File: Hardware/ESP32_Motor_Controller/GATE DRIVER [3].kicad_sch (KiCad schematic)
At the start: 42 parts, among them U301 DRV8302DCAR

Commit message: Test firmware
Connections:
- net PVDD: now also C314.1, C315.1, U301.53 (PVDD2), U301.54 (PVDD2)
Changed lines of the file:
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@@
+	)
+	(symbol
+		(lib_id "power:VSS")
+		(at 143.51 66.04 0)
+		(unit 1)
+		(exclude_from_sim no)
+		(in_bom yes)
+		(on_board yes)
+		(dnp no)
+		(property "Reference" "#PWR094"
+			(at 143.51 69.85 0)
+			(effects
+				(font
+					(size 1.27 1.27)
+				)
+				(hide yes)
+			)
+		)
+		(property "Value" "PVDD"
+			(at 147.32 64.516 0)
+			(effects
+				(font
+					(size 1.27 1.27)
+				)
+			)
+		)
+		(property "Footprint" ""
+			(at 143.51 66.04 0)
+			(effects
+				(font
+					(size 1.27 1.27)
+				)
+				(hide yes)
+			)
+		)
+		(property "Datasheet" ""
+			(at 143.51 66.04 0)
+			(effects
+				(font
+					(size 1.27 1.27)
+				)
+				(hide yes)
+			)
+		)
+		(property "Description" "Power symbol creates a global label with name \"VSS\""
+			(at 143.51 66.04 0)
+			(effects
+				(font
+					(size 1.27 1.27)
+				)
+				(hide yes)
+			)
+		)
+		(pin "1"
+		)
+		(instances
+			(project "ESP32_Motor_Controller"
+				(path "/4b1fdcf1-a19d-4728-9a21-4ed82cf33882/b48d869c-27f1-41d9-9235-2b29afe5c618"
+					(reference "#PWR094")
+					(unit 1)
+				)
+			)
+		)
 	)
 	(symbol
@@
 		(dnp no)
 		(property "Reference" "C315"
-			(at 140.716 64.262 0)
-			(effects
-				(font
+			(at 137.16 74.168 0)
+			(effects
+				(font

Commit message: PCB V2, CAD V3 & Code
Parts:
- C302, C311, C312, C313, C314, C315: footprint Capacitor_SMD:C_0402_1005Metric -> Capacitor_SMD:C_0805_2012Metric
- C320: footprint Capacitor_SMD:C_0402_1005Metric -> Capacitor_SMD:C_0603_1608Metric
- R311: value 3.3k -> 6.8k
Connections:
- net AGND: now also U301.28 (AGND)
- net at C313.1, U301.27 (AVDD): no longer U301.28 (AGND)
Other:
- note added: "90A x 2.4mΩ = 0.22V"
- note removed: "40A x 2.4mΩ = 0.1V"
- moved on the sheet: C313
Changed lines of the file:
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@@
 		)
 	)
-	(text "40A x 2.4mΩ = 0.1V\n"
+	(text "90A x 2.4mΩ = 0.22V\n"
 		(exclude_from_sim no)
 		(at 50.8 101.6 0)
@@
 	)
 	(junction
+		(at 147.32 156.21)
+		(diameter 0)
+		(color 0 0 0 0)
+	)
+	(junction
 		(at 64.77 60.96)
 		(diameter 0)
@@
 	)
 	(junction
-		(at 147.32 151.13)
-		(diameter 0)
-		(color 0 0 0 0)
-	)
-	(junction
 		(at 180.34 58.42)
 		(diameter 0)
@@
 	(wire
 		(pts
-			(xy 138.43 151.13) (xy 147.32 151.13)
+			(xy 62.23 107.95) (xy 92.71 107.95)
 		)
 		(stroke
@@
 	(wire
 		(pts
-			(xy 62.23 107.95) (xy 92.71 107.95)
+			(xy 147.32 156.21) (xy 147.32 158.75)
 		)
 		(stroke
@@
 	(wire
 		(pts
+			(xy 147.32 153.67) (xy 147.32 156.21)
+		)
+		(stroke
+			(width 0)
+			(type default)
+		)
+	)
+	(wire
+		(pts
 			(xy 29.21 102.87) (xy 41.91 102.87)
 		)
@@
 	(wire
 		(pts
+			(xy 138.43 151.13) (xy 143.51 151.13)
+		)
+		(stroke
+			(width 0)
+			(type default)
+		)
+	)
+	(wire
+		(pts
 			(xy 66.04 45.72) (xy 72.39 45.72)
 		)
@@
 	(wire
 		(pts
+			(xy 143.51 151.13) (xy 143.51 156.21)
+		)
+		(stroke
+			(width 0)
+			(type default)
+		)
+	)
+	(wire
+		(pts
 			(xy 80.01 68.58) (xy 80.01 69.85)
 		)
@@
 	(wire
 		(pts
-			(xy 161.29 87.63) (xy 170.18 87.63)
+			(xy 143.51 57.15) (xy 143.51 66.04)
 		)
 		(stroke
@@
 	(wire
 		(pts
-			(xy 147.32 148.59) (xy 147.32 151.13)
+			(xy 161.29 87.63) (xy 170.18 87.63)
 		)
 		(stroke
@@
 	(wire
 		(pts
-			(xy 147.32 151.13) (xy 147.32 153.67)
+			(xy 180.34 66.04) (xy 180.34 64.77)
 		)
 		(stroke
@@
 	(wire
 		(pts
-			(xy 180.34 66.04) (xy 180.34 64.77)
+			(xy 62.23 128.27) (xy 62.23 129.54)
 		)
 		(stroke
@@
 	(wire
 		(pts
-			(xy 62.23 128.27) (xy 62.23 129.54)
+			(xy 156.21 74.93) (xy 156.21 76.2)
 		)
 		(stroke
@@
 	(wire
 		(pts
-			(xy 156.21 74.93) (xy 156.21 76.2)
+			(xy 138.43 121.92) (xy 139.7 121.92)
 		)
 		(stroke
@@
 	(wire
 		(pts
-			(xy 138.43 121.92) (xy 139.7 121.92)
+			(xy 167.64 107.95) (xy 167.64 110.49)
 		)
 		(stroke
@@
 	(wire
 		(pts
-			(xy 167.64 107.95) (xy 167.64 110.49)
+			(xy 64.77 68.58) (xy 64.77 69.85)
 		)
 		(stroke
@@
 	(wire
 		(pts
-			(xy 64.77 68.58) (xy 64.77 69.85)
+			(xy 146.05 72.39) (xy 146.05 71.12)
 		)
 		(stroke
@@
 	(wire
 		(pts
-			(xy 146.05 72.39) (xy 146.05 71.12)
+			(xy 143.51 156.21) (xy 147.32 156.21)
 		)
 		(stroke
@@
 	(symbol
 		(lib_id "power:VSS")
-		(at 143.51 66.04 0)
+		(at 143.51 57.15 0)
 		(unit 1)
 		(exclude_from_sim no)
@@
 		(dnp no)
 		(property "Reference" "#PWR094"
-			(at 143.51 69.85 0)
+			(at 143.51 60.96 0)
 			(effects
 				(font
@@
 		)
 		(property "Value" "PVDD"
-			(at 147.32 64.516 0)
+			(at 147.32 55.626 0)
 			(effects
 				(font
@@
 		)
 		(property "Footprint" ""
-			(at 143.51 66.04 0)
+			(at 143.51 57.15 0)
 			(effects
 				(font
@@
 		)
 		(property "Datasheet" ""
-			(at 143.51 66.04 0)
+			(at 143.51 57.15 0)
 			(effects
 				(font
@@
 		)
 		(property "Description" "Power symbol creates a global label with name \"VSS\""
-			(at 143.51 66.04 0)
+			(at 143.51 57.15 0)
 			(effects
 				(font
@@
 			)
 		)
-		(property "Footprint" "Capacitor_SMD:C_0402_1005Metric"
+		(property "Footprint" "Capacitor_SMD:C_0805_2012Metric"
 			(at 143.51 68.58 0)
 			(effects
@@
 			)
 		)
-		(property "Value" "3.3k"
+		(property "Value" "6.8k"
 			(at 34.544 108.204 0)
 			(effects
@@
 			)
 		)
-		(property "Footprint" "Capacitor_SMD:C_0402_1005Metric"
+		(property "Footprint" "Capacitor_SMD:C_0805_2012Metric"
 			(at 175.26 62.23 0)
 			(effects
@@
 			)
 		)
-		(property "Footprint" "Capacitor_SMD:C_0402_1005Metric"
+		(property "Footprint" "Capacitor_SMD:C_0603_1608Metric"
 			(at 156.21 151.13 0)
 			(effects
@@
 	(symbol
 		(lib_id "Device:C_Small")
-		(at 147.32 156.21 0)
+		(at 147.32 151.13 0)
 		(unit 1)
 		(exclude_from_sim no)
@@
 		(on_board yes)
 		(dnp no)
-		(fields_autoplaced yes)
 		(property "Reference" "C313"
-			(at 149.86 154.9462 0)
+			(at 148.844 149.606 0)
 			(effects
 				(font
@@
 		)
 		(property "Value" "1uF"
-			(at 149.86 157.4862 0)
+			(at 149.606 152.146 0)
 			(effects
 				(font
@@
 			)
 		)
-		(property "Footprint" "Capacitor_SMD:C_0402_1005Metric"
-			(at 147.32 156.21 0)
+		(property "Footprint" "Capacitor_SMD:C_0805_2012Metric"
+			(at 147.32 151.13 0)
 			(effects
 				(font
@@
 		)
 		(property "Datasheet" "~"
-			(at 147.32 156.21 0)
+			(at 147.32 151.13 0)
 			(effects
 				(font
@@
 		)
 		(property "Description" "Unpolarized capacitor, small symbol"
-			(at 147.32 156.21 0)
+			(at 147.32 151.13 0)
 			(effects
 				(font
@@
 			)
 		)
-		(property "Footprint" "Capacitor_SMD:C_0402_1005Metric"
+		(property "Footprint" "Capacitor_SMD:C_0805_2012Metric"
 			(at 148.59 68.58 0)
 			(effects
@@
 			)
 		)
-		(property "Footprint" "Capacitor_SMD:C_0402_1005Metric"
+		(property "Footprint" "Capacitor_SMD:C_0805_2012Metric"
 			(at 180.34 62.23 0)
 			(effects
@@
 			)
 		)
-		(property "Footprint" "Capacitor_SMD:C_0402_1005Metric"
+		(property "Footprint" "Capacitor_SMD:C_0805_2012Metric"
 			(at 158.75 62.23 0)
 			(effects

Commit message: Code update
Motor moving
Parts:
- R308: value 10k -> 3.3k
- R309: value 52.3k -> 10k
- R310: value 100k -> 55k
- R311: value 6.8k -> 4.7k
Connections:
- net +3.3V: now also R309.1
- net 5V: no longer R309.1
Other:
- note added: "Recommended 0.8V (92% - 109%)"
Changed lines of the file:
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@@
 		)
 	)
+	(text "Recommended 0.8V (92% - 109%)"
+		(exclude_from_sim no)
+		(at 43.18 141.224 0)
+		(effects
+			(font
+				(size 0.635 0.635)
+			)
+		)
+	)
 	(text "90A x 2.4mΩ = 0.22V\n"
 		(exclude_from_sim no)
@@
 			)
 		)
-		(property "Value" "VCC"
+		(property "Value" "+3.3V"
 			(at 62.23 123.952 0)
 			(effects
@@
 			)
 		)
-		(property "Value" "6.8k"
+		(property "Value" "4.7k"
 			(at 34.544 108.204 0)
 			(effects
@@
 			)
 		)
-		(property "Value" "100k"
+		(property "Value" "55k"
 			(at 34.544 100.584 0)
 			(effects
@@
 			)
 		)
-		(property "Value" "10k"
+		(property "Value" "3.3k"
 			(at 54.864 145.034 0)
 			(effects
@@
 			)
 		)
-		(property "Value" "52.3k"
+		(property "Value" "10k"
 			(at 54.864 134.874 0)
 			(effects

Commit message: PCB_V2
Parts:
- added TP15: AVDD, TestPoint:TestPoint_Pad_D1.0mm, symbol Connector:TestPoint
- added TP17: GVDD, TestPoint:TestPoint_Pad_D1.0mm, symbol Connector:TestPoint
- C302: footprint Capacitor_SMD:C_0805_2012Metric -> Capacitor_SMD:C_0603_1608Metric
- C313: value 1uF -> 2.2uF
- C316: footprint Capacitor_SMD:C_0603_1608Metric -> Capacitor_SMD:C_0805_2012Metric
- C317: value 1.6nF -> 1.5nF
- C319: value 49uF -> 47uF
- D301: value B330 -> B360
- R301, R302: value 56 -> 56R
- R310: value 55k -> 100k
- R311: value 4.7k -> 3.3k
- R313: value 68k -> 100k
- TP7: footprint TestPoint:TestPoint_Pad_D1.5mm -> TestPoint:TestPoint_Pad_D1mm
- TP8: footprint TestPoint:TestPoint_Pad_D1.5mm -> TestPoint:TestPoint_Pad_D1.0mm
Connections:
- net SP_1 is gone; now on net AGND: U301.32 (SP1)
- net SP_2 is gone; now on net AGND: U301.30 (SP2)
- net AVDD: now reaches C313.1, U301.27 (AVDD)
- net AVDD: now also TP15.1
- net GVDD: now reaches C302.1, U301.13 (GVDD)
- net GVDD: now also TP17.1
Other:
- note added: "22uH for 36V"
- note added: "40A x 2.4mΩ = 0.1V"
- note removed: "90A x 2.4mΩ = 0.22V"
- note removed: "TEST - MAY BE ADJUST"
- company: (none) -> ANGEL PELEGRY VELASCO
- moved on the sheet: C302, C303, C304, C305, C311, C312, C313, C314, C315, C320, R303, R304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

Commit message: Buck Components Update
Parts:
- C317: value 1.5nF -> 15pF; footprint Capacitor_SMD:C_0402_1005Metric -> Capacitor_SMD:C_0603_1608Metric
- C318: value 36pF -> 1nF
- C319: value 47uF -> 12uH; footprint Capacitor_SMD:C_0603_1608Metric -> Capacitor_SMD:C_0805_2012Metric
- R306: value 15k -> 86.6k
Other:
- note removed: "22uH for 36V"
- moved on the sheet: C302, C303, C304, C305, C306, C307, C308, C309, C310, C311, C312, C313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

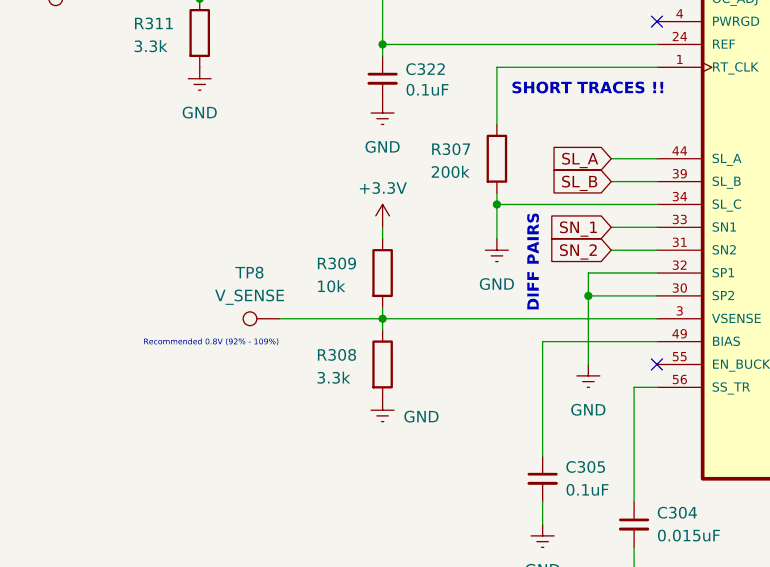
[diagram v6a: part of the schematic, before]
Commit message: CAN_Bus
MCP2551 is transmitting packets
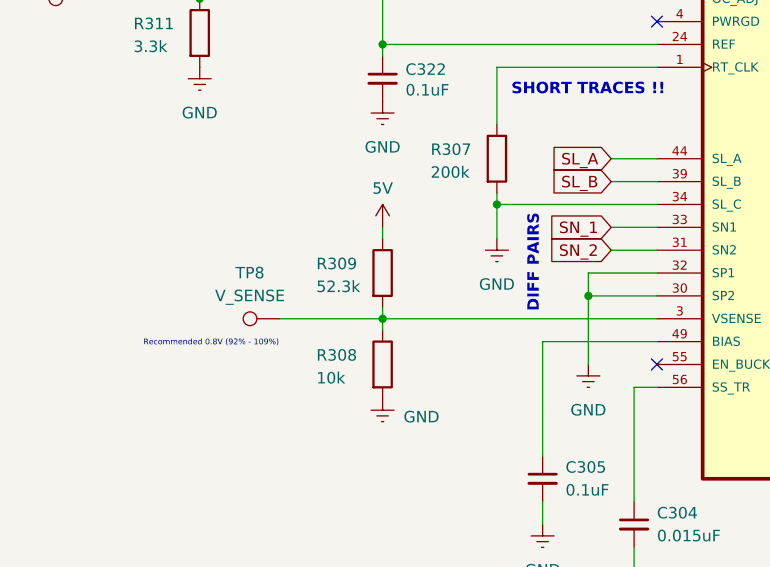
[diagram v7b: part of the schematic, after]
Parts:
- R308: value 3.3k -> 10k
- R309: value 10k -> 52.3k
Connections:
- net +3.3V: no longer R309.1
- net 5V: now also R309.1
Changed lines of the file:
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@@
 			"NQBzAHYASgBBAE8AeQBoADAAOABCADkATQBKAHQAUABpAHgAWQB0AGIAVwBsAHIARQA0AGYAUABQ"
 			"AFAAOQArADcAZAAyADkAWgBrAFEAQQBBAEEAQQBCAEEAdAB6AHcAOABQAEoANQA5ADkAbABsAHgA"
-			"SgBaADIARwBoAG8AWgAzADMAbg=="
+			"SgBaADIARwBoAG8AWgAzADMAbgAAAAAAAAAAAAAAAAAAAAAAAAAAAAAAAAAAAAAAAAAAAAAAAAAA"
+			"AAAAAAAAAAAAAAAAAAAAAAAAAAAAAAAAAAAAAAAAAAAAAAAAAAAAAAAAAAAAAAAAAAAAAAAAAAAA"
+			"AAAAAAAAAAAAAAAAAAAAAAAAAAAAAAAAAAAAAAAAAAAAAAAAAAAAAAAAAAAAAAAAAAAAAAAAAAAA"
+			"AAAAAAAAAAAAAAAAAAAAAAAAAAAAAAAAAAAAAAAAAAAAAAAAAAAAAAAAAAAAAAAAAAAAAAAAAAAA"
+			"AAAAAAAAAAAAAAAAAAAAAAAAAAAAAAAAAAAAAAAAAAAAAAAAAAAAAAAAAAAAAAAAAAAAAAAAAAAA"
+			"AAAAAAAAAAAAAAAAAAAAAAAAAAAAAAAAAAAAAAAAAAAAAAAAAAAAAAAAAAAAAAAAAAAAAAAAAAAA"
+			"AAAAAAAAAAAAAAAAAAAAAAAAAAAAAAAAAAAAAAAAAAAAAAAAAAAAAAAAAAAAAAAAAAAAAAAAAAAA"
+			"AAAAAAAAAAAAAAAAAAAAAAAAAAAAAAAAAAAAAAAAAAAAAAAAAAAAAAAAAAAAAAAAAAAAAAAAAAAA"
+			"AAAAAAAAAAAAAAAAAAAAAAAAAAAAAAAAAAAAAAAAAAAAAAAAAAAAAAAAAAAAAAAAAAAAAAAAAAAA"
+			"AAAAAAAAAAAAAAAAAAAAAAAAAAAAAAAAAAAAAAAAAAAAAAAAAAAAAAAAAAAAAAAAAAAAAAAAAAAA"
+			"AAAAAAAAAAAAAAAAAAAAAAAAAAAAAAAAAAAAAAAAAAAAAAAAAAAAAAAAAAAAAAAAAAAAAAAAAAAA"
+			"AAAAAAAAAAAAAAAAAAAAAAAAAAAAAAAAAAAAAAAAAAAAAAAAAAAAAAAAAAAAAAAAAAAAAAAAAAAA"
+			"AAAAAAAAAAAAAAAAAAAAAAAAAAAAAAAAAAAAAAAAAAAAAAAAAAAAAAAAAAAAAAAAAAAAAAAAAAAA"
+			"AAAAAAAAAAAAAAAAAAAAAAAAAAAAAAAAAAAAAAAAAAAAAAAAAAAAAAAAAAAAAAAAAAAAAAAAAAAA"
+			"AAAAAAAAAAAAAAAAAAAAAAAAAAAAAAAAAAAAAAAAAAAAAAAAAAAAAAAAAAAAAAAAAAAAAAAAAAAA"
+			"AAAAAAAAAAAAAAAAAAAAAAAAAAAAAAAAAAAAAAAAAAAAAAAAAAAAAAAAAAAAAAAAAAAAAAAAAAAA"
+			"AAAAAAAAAAAAAAAAAAAAAAAAAAAAAAAAAAAAAAAAAAAAAAAAAAAAAAAAAAAAAAAAAAAAAAAAAAAA"
+			"AAAAAAAAAAAAAAAAAAAAAAAAAAAAAAAAAAAAAAAAAAAAAAAAAAAAAAAAAAAAAAAAAAAAAAAAAAAA"
+			"AAAAAAAAAAAAAAAAAAAAAAAAAA=="
 		)
 	)
@@
 			)
 		)
-		(property "Value" "+3.3V"
+		(property "Value" "5V"
 			(at 74.93 127.762 0)
 			(effects
@@
 			)
 		)
-		(property "Value" "3.3k"
+		(property "Value" "10k"
 			(at 67.564 148.844 0)
 			(effects
@@
 			)
 		)
-		(property "Value" "10k"
+		(property "Value" "52.3k"
 			(at 67.564 138.684 0)
 			(effects
